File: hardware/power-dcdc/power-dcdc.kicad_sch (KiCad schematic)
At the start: 65 parts, among them J1 SOLAR_IN, J2 BATT2, J3 BATT1, J4 DCDC-MEASURES, J5 DCDC-PWM, Q1 SIR164ADP, Q2 SIR164ADP, Q3 SI7149ADP, Q4 SI7149ADP, Q5 SI7149ADP, Q6 SI7149ADP, U1 LP4951C, U2 NCP5901B, U3 PAC1953-1, U4 DGD0215, U5 DGD0215

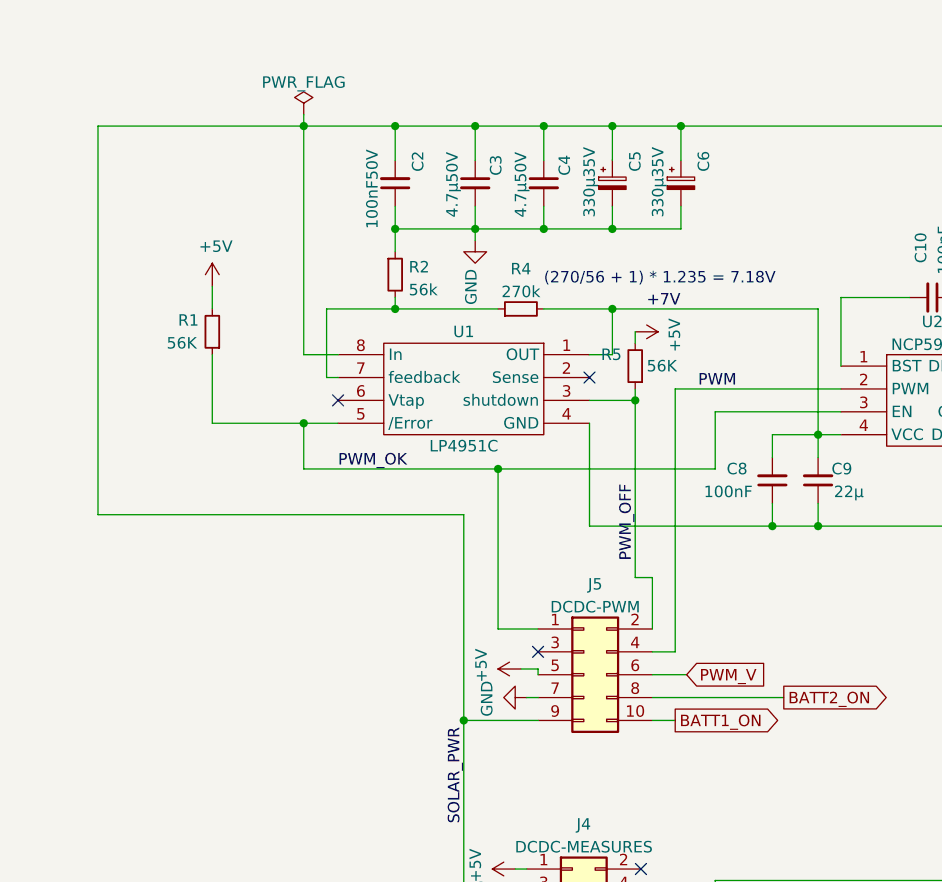
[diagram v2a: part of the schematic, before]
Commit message: Finish routing the power board
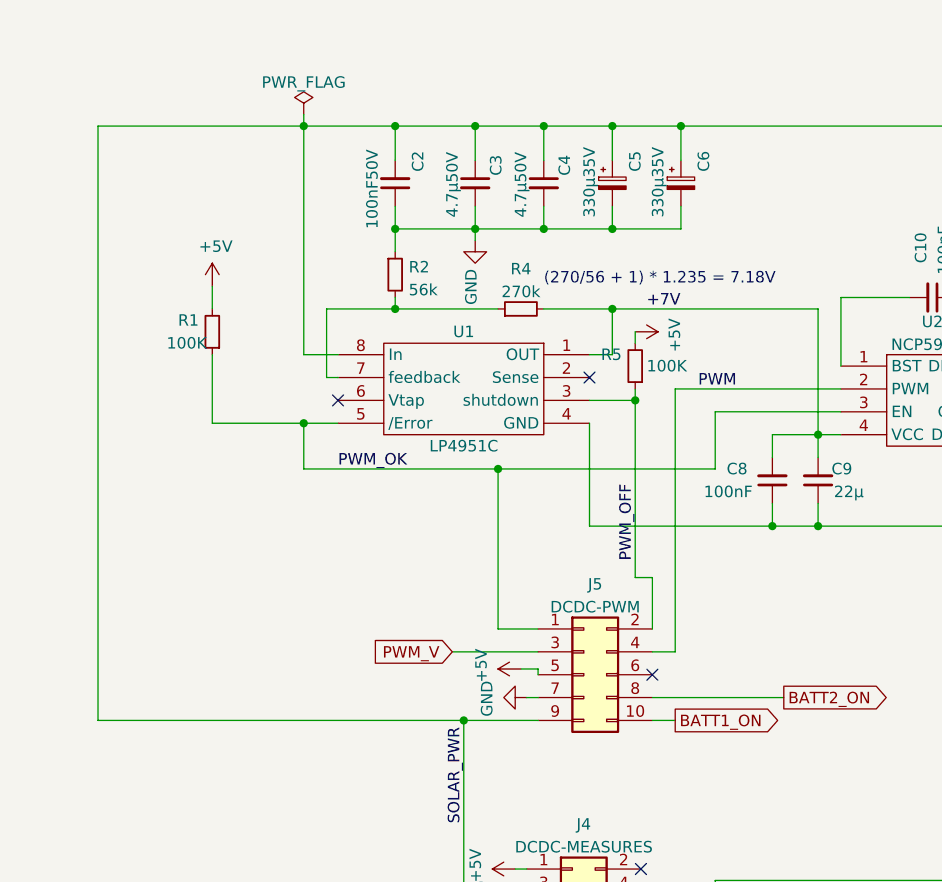
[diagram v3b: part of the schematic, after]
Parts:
- J4, J5: footprint (none) -> Connector_PinSocket_2.54mm:PinSocket_2x05_P2.54mm_Vertical
- R1, R5: value 56K -> 100K; footprint Resistor_SMD:R_1206_3216Metric_Pad1.30x1.75mm_HandSolder -> Resistor_THT:R_Axial_DIN0309_L9.0mm_D3.2mm_P12.70mm_Horizontal
- R7, R9: footprint Resistor_SMD:R_0805_2012Metric_Pad1.20x1.40mm_HandSolder -> Resistor_THT:R_Axial_DIN0309_L9.0mm_D3.2mm_P12.70mm_Horizontal
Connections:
- net PWM_V: now also J5.3 (Pin_3); no longer J5.6 (Pin_6)
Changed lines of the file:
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@@
   (junction (at 162.56 73.66) (diameter 0) (color 0 0 0 0)
   )
-  (no_connect (at 88.265 87.63))
   (no_connect (at 86.995 116.84))
   (no_connect (at 99.695 114.3))
+  (no_connect (at 100.965 90.17))
   (no_connect (at 99.695 111.76))
   (no_connect (at 66.04 59.69))
@@
     (stroke (width 0) (type default) (color 0 0 0 0))
   )
+  (wire (pts (xy 80.01 95.25) (xy 39.37 95.25))
+    (stroke (width 0) (type default) (color 0 0 0 0))
+  )
   (wire (pts (xy 167.005 113.03) (xy 107.95 113.03))
     (stroke (width 0) (type default) (color 0 0 0 0))
@@
     (stroke (width 0) (type default) (color 0 0 0 0))
   )
-  (wire (pts (xy 80.01 72.39) (xy 39.37 72.39))
-    (stroke (width 0) (type default) (color 0 0 0 0))
-  )
   (wire (pts (xy 224.79 68.58) (xy 224.79 83.82))
     (stroke (width 0) (type default) (color 0 0 0 0))
@@
     (stroke (width 0) (type default) (color 0 0 0 0))
   )
+  (wire (pts (xy 78.74 87.63) (xy 88.265 87.63))
+    (stroke (width 0) (type default) (color 0 0 0 0))
+  )
   (wire (pts (xy 245.11 129.54) (xy 250.19 129.54))
     (stroke (width 0) (type default) (color 0 0 0 0))
@@
     (stroke (width 0) (type default) (color 0 0 0 0))
   )
-  (wire (pts (xy 39.37 72.39) (xy 39.37 29.21))
-    (stroke (width 0) (type default) (color 0 0 0 0))
-  )
   (wire (pts (xy 88.265 85.09) (xy 83.82 85.09))
     (stroke (width 0) (type default) (color 0 0 0 0))
@@
     (stroke (width 0) (type default) (color 0 0 0 0))
   )
+  (wire (pts (xy 39.37 29.21) (xy 39.37 95.25))
+    (stroke (width 0) (type default) (color 0 0 0 0))
+  )
   (wire (pts (xy 205.74 134.62) (xy 205.74 132.08))
     (stroke (width 0) (type default) (color 0 0 0 0))
@@
     (stroke (width 0) (type default) (color 0 0 0 0))
   )
-  (wire (pts (xy 100.965 90.17) (xy 104.775 90.17))
-    (stroke (width 0) (type default) (color 0 0 0 0))
-  )
   (wire (pts (xy 234.95 129.54) (xy 236.22 129.54))
     (stroke (width 0) (type default) (color 0 0 0 0))
@@
   )
   (wire (pts (xy 119.38 142.24) (xy 114.3 142.24))
-    (stroke (width 0) (type default) (color 0 0 0 0))
-  )
-  (wire (pts (xy 80.01 72.39) (xy 80.01 95.25))
     (stroke (width 0) (type default) (color 0 0 0 0))
   )
@@
     (effects (font (size 1.27 1.27)) (justify left bottom))
   )
-  (global_label "PWM_V" (shape input) (at 104.775 90.17 0) (fields_autoplaced)
-    (effects (font (size 1.27 1.27)) (justify left))
-    (property "Intersheet References" "${INTERSHEET_REFS}" (id 0) (at 113.4171 90.0906 0)
-      (effects (font (size 1.27 1.27)) (justify left) hide)
+  (global_label "PWM_V" (shape input) (at 78.74 87.63 180) (fields_autoplaced)
+    (effects (font (size 1.27 1.27)) (justify right))
+    (property "Intersheet References" "${INTERSHEET_REFS}" (id 0) (at 70.0979 87.7094 0)
+      (effects (font (size 1.27 1.27)) (justify right) hide)
     )
   )
@@
       (effects (font (size 1.27 1.27)) (justify right))
     )
-    (property "Footprint" "Resistor_SMD:R_0805_2012Metric_Pad1.20x1.40mm_HandSolder" (id 2) (at 118.11 124.46 0)
+    (property "Footprint" "Resistor_THT:R_Axial_DIN0309_L9.0mm_D3.2mm_P12.70mm_Horizontal" (id 2) (at 118.11 124.46 0)
       (effects (font (size 1.27 1.27)) hide)
     )
@@
       (effects (font (size 1.27 1.27)) (justify right))
     )
-    (property "Footprint" "Resistor_SMD:R_0805_2012Metric_Pad1.20x1.40mm_HandSolder" (id 2) (at 173.99 124.46 0)
+    (property "Footprint" "Resistor_THT:R_Axial_DIN0309_L9.0mm_D3.2mm_P12.70mm_Horizontal" (id 2) (at 173.99 124.46 0)
       (effects (font (size 1.27 1.27)) hide)
     )
@@
       (effects (font (size 1.27 1.27)) (justify right))
     )
-    (property "Value" "56K" (id 1) (at 46.99 53.34 0)
-      (effects (font (size 1.27 1.27)) (justify right))
-    )
-    (property "Footprint" "Resistor_SMD:R_1206_3216Metric_Pad1.30x1.75mm_HandSolder" (id 2) (at 52.07 52.07 0)
+    (property "Value" "100K" (id 1) (at 46.99 53.34 0)
+      (effects (font (size 1.27 1.27)) (justify right))
+    )
+    (property "Footprint" "Resistor_THT:R_Axial_DIN0309_L9.0mm_D3.2mm_P12.70mm_Horizontal" (id 2) (at 52.07 52.07 0)
       (effects (font (size 1.27 1.27)) hide)
     )
@@
       (effects (font (size 1.27 1.27)) (justify right))
     )
-    (property "Value" "56K" (id 1) (at 100.33 55.88 0)
-      (effects (font (size 1.27 1.27)) (justify right))
-    )
-    (property "Footprint" "Resistor_SMD:R_1206_3216Metric_Pad1.30x1.75mm_HandSolder" (id 2) (at 99.06 55.88 0)
+    (property "Value" "100K" (id 1) (at 100.33 55.88 0)
+      (effects (font (size 1.27 1.27)) (justify right))
+    )
+    (property "Footprint" "Resistor_THT:R_Axial_DIN0309_L9.0mm_D3.2mm_P12.70mm_Horizontal" (id 2) (at 99.06 55.88 0)
       (effects (font (size 1.27 1.27)) hide)
     )
@@
     (property "Reference" "J5" (id 0) (at 94.615 80.1202 0))
     (property "Value" "DCDC-PWM" (id 1) (at 94.615 82.6571 0))
-    (property "Footprint" "" (id 2) (at 93.345 90.17 0)
+    (property "Footprint" "Connector_PinSocket_2.54mm:PinSocket_2x05_P2.54mm_Vertical" (id 2) (at 93.345 90.17 0)
       (effects (font (size 1.27 1.27)) hide)
     )
@@
     (property "Reference" "J4" (id 0) (at 93.345 106.7902 0))
     (property "Value" "DCDC-MEASURES" (id 1) (at 93.345 109.3271 0))
-    (property "Footprint" "" (id 2) (at 92.075 116.84 0)
+    (property "Footprint" "Connector_PinSocket_2.54mm:PinSocket_2x05_P2.54mm_Vertical" (id 2) (at 92.075 116.84 0)
       (effects (font (size 1.27 1.27)) hide)
     )
@@
     )
     (path "/fccac9cc-0228-4cd7-8ab6-af46139694cd"
-      (reference "J4") (unit 1) (value "DCDC-MEASURES") (footprint "")
+      (reference "J4") (unit 1) (value "DCDC-MEASURES") (footprint "Connector_PinSocket_2.54mm:PinSocket_2x05_P2.54mm_Vertical")
     )
     (path "/d8e1ba90-0050-486c-92d5-5b39e8cd29cd"
-      (reference "J5") (unit 1) (value "DCDC-PWM") (footprint "")
+      (reference "J5") (unit 1) (value "DCDC-PWM") (footprint "Connector_PinSocket_2.54mm:PinSocket_2x05_P2.54mm_Vertical")
     )
     (path "/ec966962-cf8a-4185-86dd-e01695d363d1"
@@
     )
     (path "/7b026b96-3724-4b2a-8670-c7ca9e962129"
-      (reference "R1") (unit 1) (value "56K") (footprint "Resistor_SMD:R_1206_3216Metric_Pad1.30x1.75mm_HandSolder")
+      (reference "R1") (unit 1) (value "100K") (footprint "Resistor_THT:R_Axial_DIN0309_L9.0mm_D3.2mm_P12.70mm_Horizontal")
     )
     (path "/af2b0fb0-1c42-4881-be14-8efcd2d1c801"
@@
     )
     (path "/9d57c1ba-3976-407f-8594-55ec91182989"
-      (reference "R5") (unit 1) (value "56K") (footprint "Resistor_SMD:R_1206_3216Metric_Pad1.30x1.75mm_HandSolder")
+      (reference "R5") (unit 1) (value "100K") (footprint "Resistor_THT:R_Axial_DIN0309_L9.0mm_D3.2mm_P12.70mm_Horizontal")
     )
     (path "/bb0dbdc9-e52a-441d-adb6-3de3aa546cee"
@@
     )
     (path "/1e11e7ee-1d09-4317-81f3-9082abf4db7f"
-      (reference "R7") (unit 1) (value "10K") (footprint "Resistor_SMD:R_0805_2012Metric_Pad1.20x1.40mm_HandSolder")
+      (reference "R7") (unit 1) (value "10K") (footprint "Resistor_THT:R_Axial_DIN0309_L9.0mm_D3.2mm_P12.70mm_Horizontal")
     )
     (path "/47f33c80-6210-49e0-abe8-9697abdd5dd8"
@@
     )
     (path "/4f70259a-7e96-41a9-9e7d-3bf8781b99e6"
-      (reference "R9") (unit 1) (value "10K") (footprint "Resistor_SMD:R_0805_2012Metric_Pad1.20x1.40mm_HandSolder")
+      (reference "R9") (unit 1) (value "10K") (footprint "Resistor_THT:R_Axial_DIN0309_L9.0mm_D3.2mm_P12.70mm_Horizontal")
     )
     (path "/c1a93191-2484-4f2d-b59b-5c24507bbe1b"
